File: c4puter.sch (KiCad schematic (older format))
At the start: 1 part, among them J7 19V 3A

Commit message: Uh, more misc work.
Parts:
- added C1: 1u, IPC7351-Nominal:CAPC2012X70, symbol C-0805
- added C2: 100n, IPC7351-Nominal:CAPC1005X55, symbol C-0402
- added Q1, Q2: AOD4189, smd-semi:TO-252, symbol AOD4189
- added R1: 100k, IPC7351-Nominal:RESC1608X50, symbol R-0603
- added R2: 330k, IPC7351-Nominal:RESC1608X50, symbol R-0603
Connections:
- net labels added: +12, 12VIN
- net labels removed: V+
- wire segments 22 -> 41
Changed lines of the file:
@@
 $Descr A4 11693 8268
 encoding utf-8
-Sheet 1 8
+Sheet 1 9
 Title ""
 Date ""
@@
 $EndComp
 Wire Wire Line
-	1200 800  1300 800
-$Comp
-L V+ #PWR2
-U 1 1 5765EDAE
-P 1300 800
-F 0 "#PWR2" H 1300 850 30  0001 C CNN
-F 1 "V+" V 1300 888 50  0000 L CNN
-F 2 "" H 1300 800 60  0000 C CNN
-F 3 "" H 1300 800 60  0000 C CNN
-	1    1300 800
-	0    1    1    0
-$EndComp
+	1200 800  1500 800
 $Comp
 L GND #PWR1
@@
 F1 "Power.sch" 60
 $EndSheet
+$Comp
+L AOD4189 Q2
+U 1 1 577BAA66
+P 2600 850
+F 0 "Q2" V 2864 850 50  0000 C CNN
+F 1 "AOD4189" V 2773 850 50  0000 C CNN
+F 2 "smd-semi:TO-252" H 2600 600 50  0001 C CNN
+F 3 "http://aosmd.com/res/data_sheets/AOD4189.pdf" H 2600 700 60  0001 C CNN
+F 4 "PMOS AOS AOD4189" H 2600 500 60  0001 C CNN "BOM"
+	1    2600 850
+	0    -1   -1   0
+$EndComp
+$Comp
+L AOD4189 Q1
+U 1 1 577BB49C
+P 1600 850
+F 0 "Q1" V 1864 850 50  0000 C CNN
+F 1 "AOD4189" V 1773 850 50  0000 C CNN
+F 2 "smd-semi:TO-252" H 1600 600 50  0001 C CNN
+F 3 "http://aosmd.com/res/data_sheets/AOD4189.pdf" H 1600 700 60  0001 C CNN
+F 4 "PMOS AOS AOD4189" H 1600 500 60  0001 C CNN "BOM"
+	1    1600 850
+	0    1    -1   0
+$EndComp
+Wire Wire Line
+	1700 800  1850 800
+Wire Wire Line
+	1850 800  2200 800
+Wire Wire Line
+	2200 800  2500 800
+Text GLabel 3100 800  2    50   Output ~ 0
++12
+Wire Wire Line
+	2700 800  2950 800
+Wire Wire Line
+	2950 800  3100 800
+Wire Wire Line
+	1650 900  1650 1100
+Wire Wire Line
+	1650 1100 1650 1200
+Wire Wire Line
+	1650 1100 1850 1100
+Wire Wire Line
+	1850 1100 2200 1100
+Wire Wire Line
+	2200 1100 2550 1100
+Wire Wire Line
+	2550 1100 2650 1100
+Wire Wire Line
+	2550 1100 2550 900
+$Comp
+L C-0805 C1
+U 1 1 577BC70C
+P 1850 950
+F 0 "C1" H 1963 996 50  0000 L CNN
+F 1 "1u" H 1963 905 50  0000 L CNN
+F 2 "IPC7351-Nominal:CAPC2012X70" H 1850 950 50  0001 C CNN
+F 3 "" H 1840 925 60  0000 C CNN
+F 4 "CAP MLCC 1u ≥X5R 16V 20% [0805]" H 2650 1500 60  0001 C CNN "BOM"
+	1    1850 950
+	1    0    0    -1
+$EndComp
+Wire Wire Line
+	1850 850  1850 800
+Connection ~ 1850 800
+Wire Wire Line
+	1850 1050 1850 1100
+Connection ~ 1850 1100
+$Comp
+L R-0603 R1
+U 1 1 577BD3FC
+P 1650 1300
+F 0 "R1" H 1713 1346 50  0000 L CNN
+F 1 "100k" H 1713 1255 50  0000 L CNN
+F 2 "IPC7351-Nominal:RESC1608X50" H 1650 1300 50  0001 C CNN
+F 3 "" H 1650 1350 60  0000 C CNN
+F 4 "RES SMD 100k 1% [0603]" H 2400 1850 60  0001 C CNN "BOM"
+	1    1650 1300
+	1    0    0    -1
+$EndComp
+Wire Wire Line
+	2200 800  2200 850
+Connection ~ 2200 800
+Wire Wire Line
+	2200 1050 2200 1100
+Connection ~ 2200 1100
+Connection ~ 1650 1100
+$Comp
+L R-0603 R2
+U 1 1 577BD8AB
+P 2200 950
+F 0 "R2" H 2263 996 50  0000 L CNN
+F 1 "330k" H 2263 905 50  0000 L CNN
+F 2 "IPC7351-Nominal:RESC1608X50" H 2200 950 50  0001 C CNN
+F 3 "" H 2200 1000 60  0000 C CNN
+F 4 "RES SMD 330k 1% [0603]" H 2950 1500 60  0001 C CNN "BOM"
+	1    2200 950
+	1    0    0    -1
+$EndComp
+$Comp
+L GND #PWR2
+U 1 1 577BDBFF
+P 1650 1450
+F 0 "#PWR2" H 1650 1450 30  0001 C CNN
+F 1 "GND" H 1650 1380 30  0001 C CNN
+F 2 "" H 1650 1450 60  0000 C CNN
+F 3 "" H 1650 1450 60  0000 C CNN
+	1    1650 1450
+	1    0    0    -1
+$EndComp
+Wire Wire Line
+	1650 1450 1650 1400
+$Comp
+L C-0402 C2
+U 1 1 577BE5F3
+P 2750 1100
+F 0 "C2" V 2908 1100 50  0000 C CNN
+F 1 "100n" V 2999 1100 50  0000 C CNN
+F 2 "IPC7351-Nominal:CAPC1005X55" H 2750 1100 50  0001 C CNN
+F 3 "" H 2740 1075 60  0000 C CNN
+F 4 "CAP MLCC 100n ≥X5R 25V 10% [0402]" H 3550 1650 60  0001 C CNN "BOM"
+	1    2750 1100
+	0    1    1    0
+$EndComp
+Connection ~ 2550 1100
+Wire Wire Line
+	2950 800  2950 1100
+Wire Wire Line
+	2950 1100 2850 1100
+Connection ~ 2950 800
+Text Label 1250 800  0    50   ~ 0
+12VIN
+$Sheet
+S 4300 4700 1300 900
+U 577C2AEA
+F0 "Blinkenlights" 50
+F1 "Blinkenlights.sch" 50
+$EndSheet
 $EndSCHEMATC

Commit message: MOAR WORK
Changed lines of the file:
@@
 $EndComp
 Wire Wire Line
-	1700 800  1850 800
-Wire Wire Line
-	1850 800  2200 800
-Wire Wire Line
-	2200 800  2500 800
+	1700 800  2500 800
 Text GLabel 3100 800  2    50   Output ~ 0
 +12
 Wire Wire Line
-	2700 800  2950 800
+	2700 800  3100 800
 Wire Wire Line
-	2950 800  3100 800
+	1650 900  1650 1200
 Wire Wire Line
-	1650 900  1650 1100
-Wire Wire Line
-	1650 1100 1650 1200
-Wire Wire Line
-	1650 1100 1850 1100
-Wire Wire Line
-	1850 1100 2200 1100
-Wire Wire Line
-	2200 1100 2550 1100
-Wire Wire Line
-	2550 1100 2650 1100
+	1650 1100 2650 1100
 Wire Wire Line
 	2550 1100 2550 900

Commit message: MOAR WORK, v2
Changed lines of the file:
@@
 F14 "CPUASTR" B R 6100 3600 50
 F15 "CPUDSTR" B R 6100 3700 50
+F16 "LIMBD[0..7]" B L 4700 3500 50
+F17 "LIMBA15" I L 4700 3600 50
+F18 "LIMBNCS" I L 4700 3700 50
+F19 "LIMBNRD" I L 4700 3900 50
+F20 "LIMBNWAIT" O L 4700 4000 50
+F21 "LIMBNWE" I L 4700 3800 50
 $EndSheet
 $Sheet
@@
 F0 "EC" 60
 F1 "EC.sch" 60
+F2 "D[0..7]" B R 3200 4800 50
+F3 "A15" O R 3200 4900 50
+F4 "NCS" O R 3200 5000 50
+F5 "NWE" O R 3200 5100 50
+F6 "NRD" O R 3200 5200 50
+F7 "NWAIT" O R 3200 5300 50
 $EndSheet
 $Comp
@@
 F1 "Blinkenlights.sch" 50
 $EndSheet
+Wire Bus Line
+	4700 3500 3400 3500
+Wire Bus Line
+	3400 3500 3400 4800
+Wire Bus Line
+	3400 4800 3200 4800
+Wire Wire Line
+	3200 4900 3500 4900
+Wire Wire Line
+	3500 4900 3500 3600
+Wire Wire Line
+	3500 3600 4700 3600
+Wire Wire Line
+	4700 3700 3600 3700
+Wire Wire Line
+	3600 3700 3600 5000
+Wire Wire Line
+	3600 5000 3200 5000
+Wire Wire Line
+	3200 5100 3700 5100
+Wire Wire Line
+	3700 5100 3700 3800
+Wire Wire Line
+	3700 3800 4700 3800
+Wire Wire Line
+	4700 3900 3800 3900
+Wire Wire Line
+	3800 3900 3800 5200
+Wire Wire Line
+	3800 5200 3200 5200
+Wire Wire Line
+	3200 5300 3900 5300
+Wire Wire Line
+	3900 5300 3900 4000
+Wire Wire Line
+	3900 4000 4700 4000
 $EndSCHEMATC

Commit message: workworkwork
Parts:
- added MP1, MP2, MP3, MP4: SCREW, mech:SCREW-4-SUPPORTED, symbol SCREW
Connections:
- net GND: now also MP1.1, MP2.1, MP3.1, MP4.1

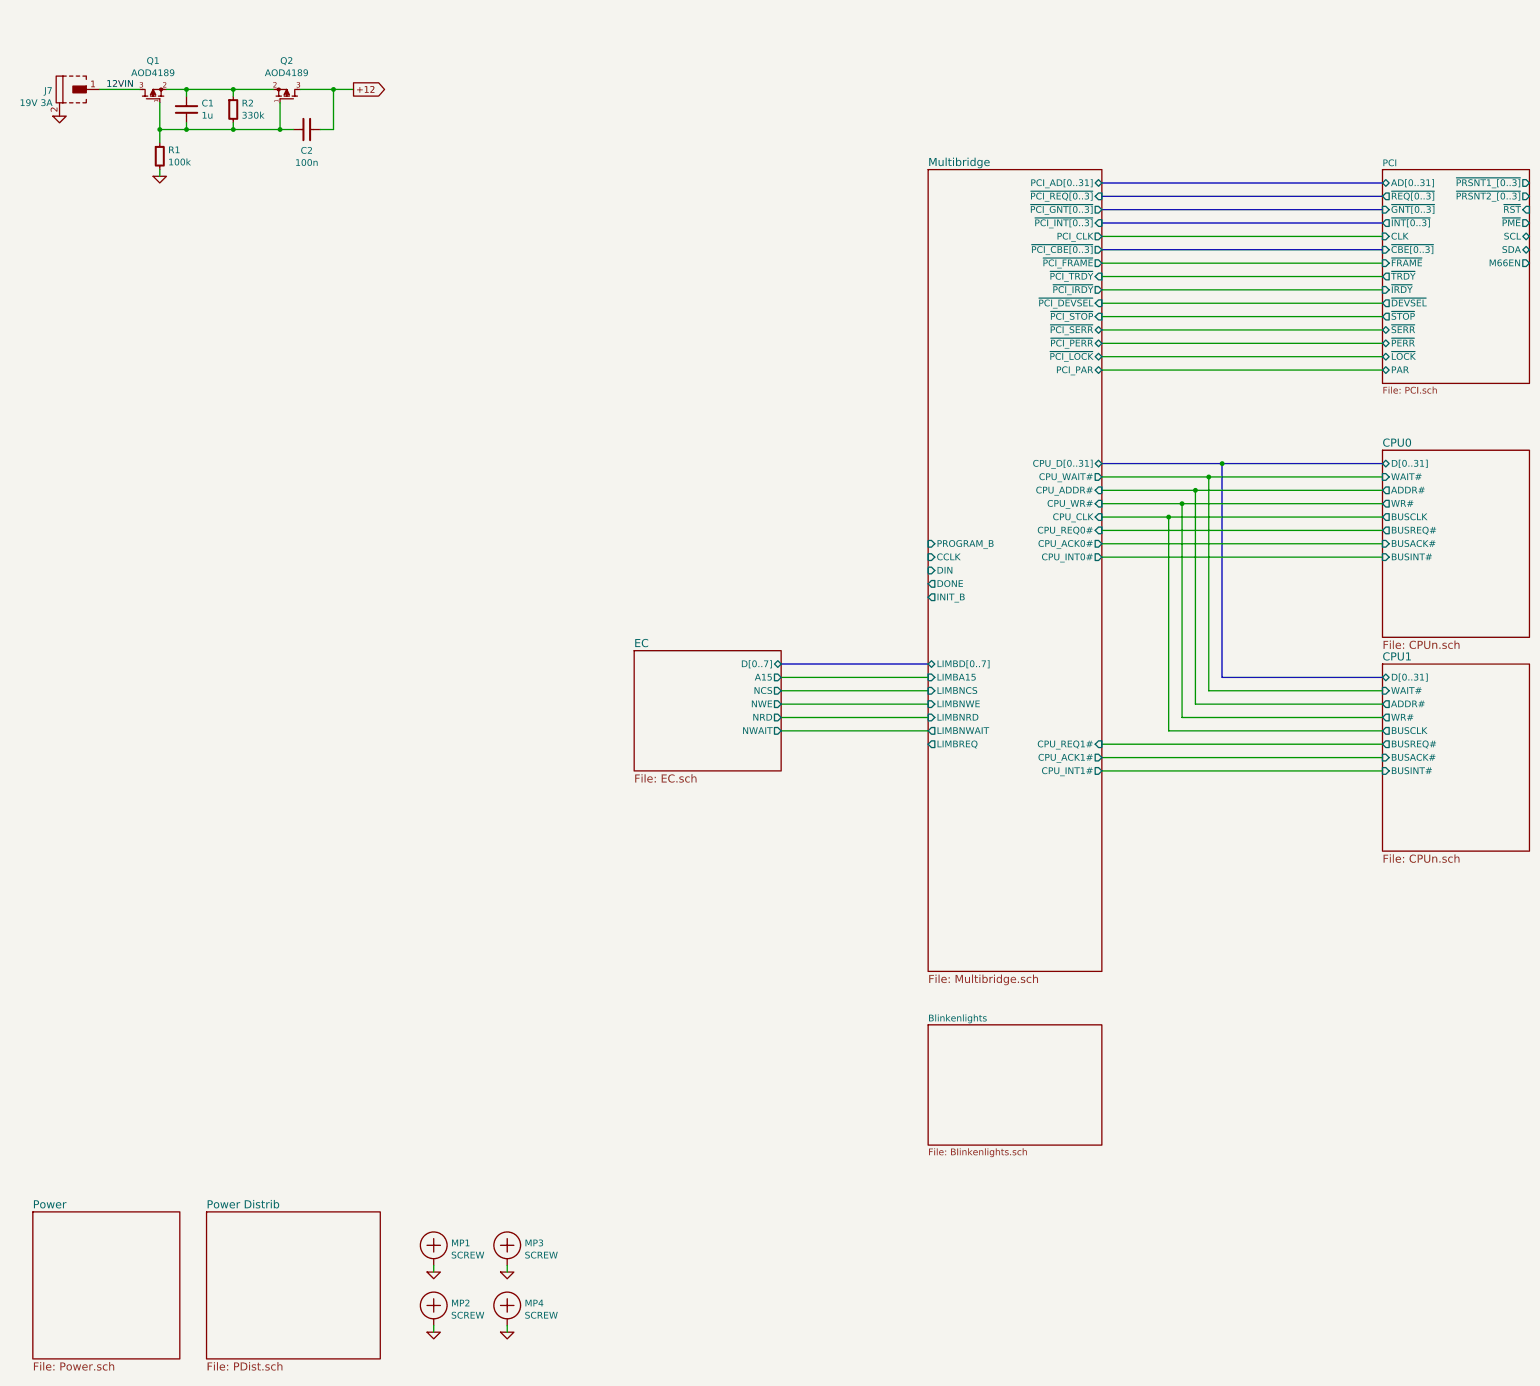
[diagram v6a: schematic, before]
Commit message: Route CPU bus and cache
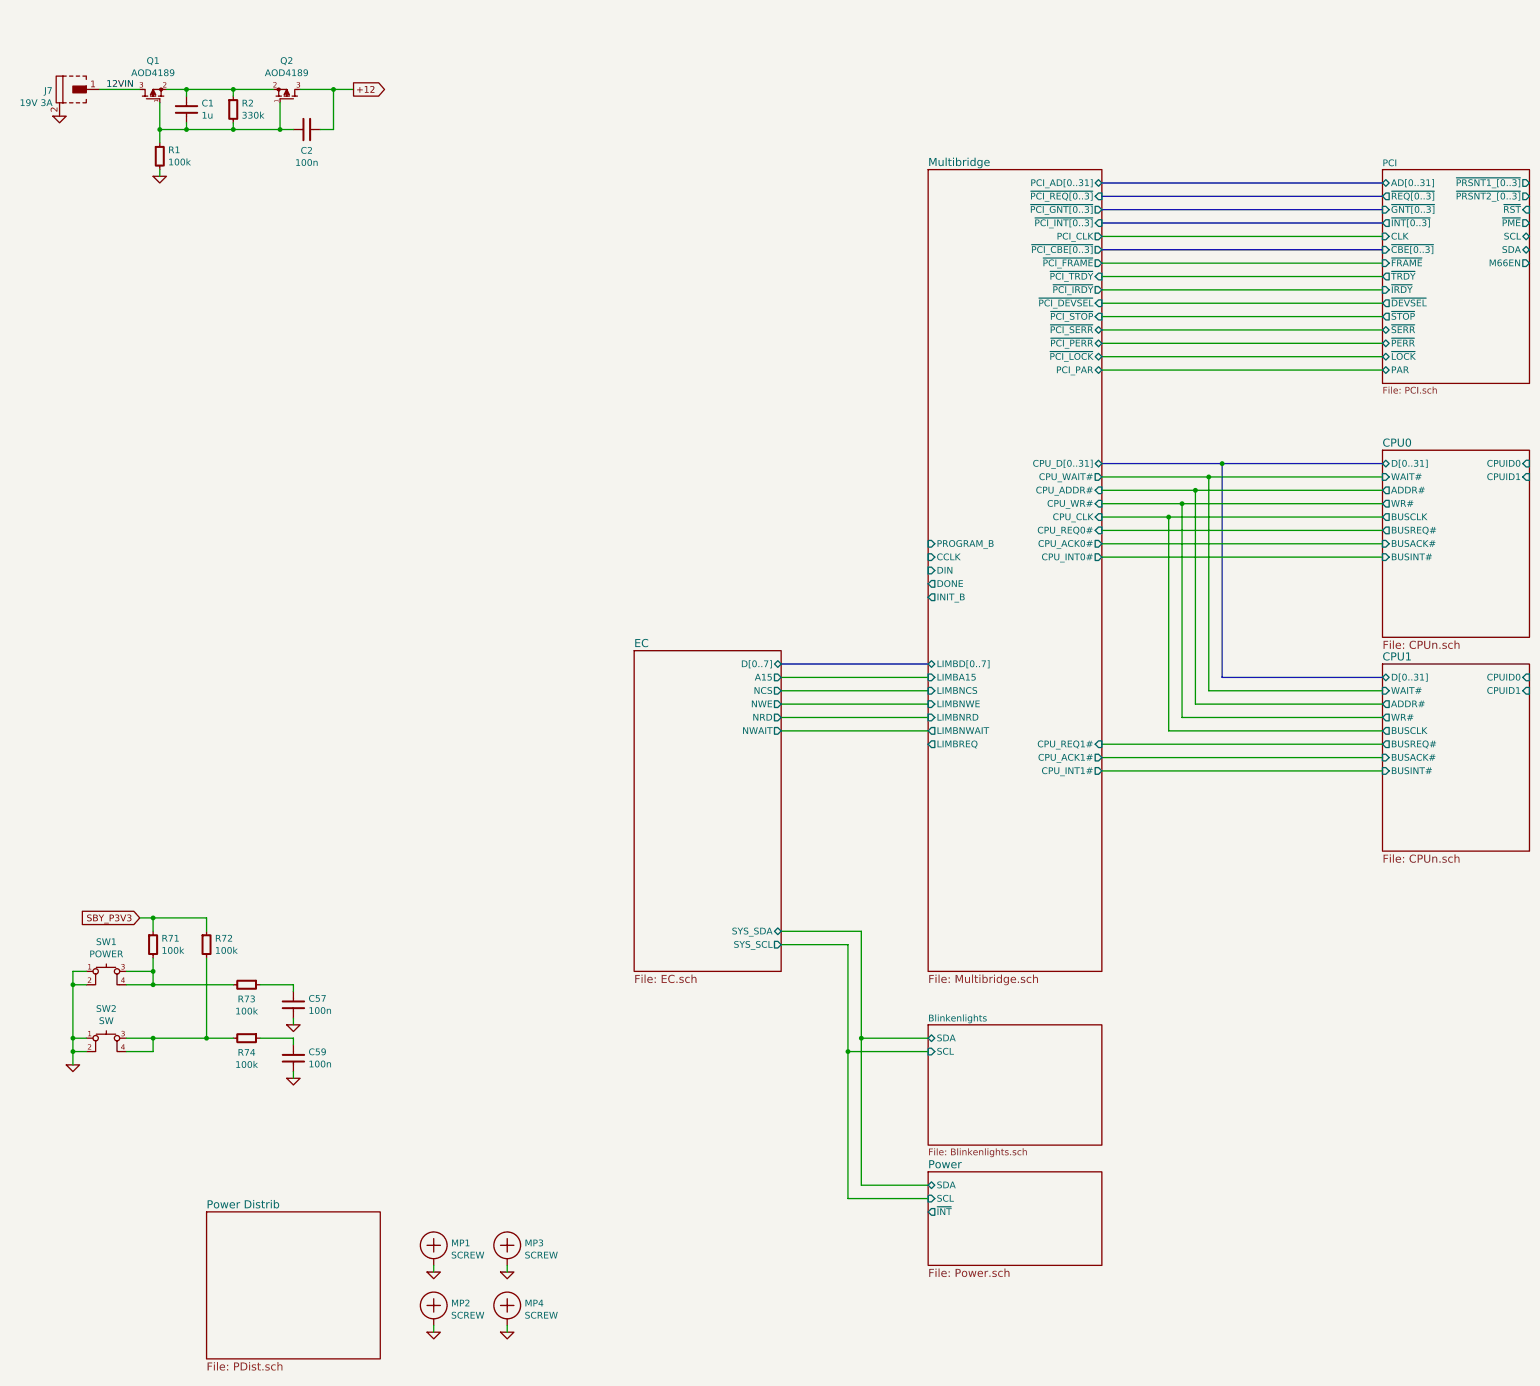
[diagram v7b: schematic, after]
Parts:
- added C57, C59: 100n, IPC7351-Nominal:CAPC1005X55, symbol C-0402
- added R71, R72, R73, R74: 100k, IPC7351-Nominal:RESC1608X50, symbol R-0603
- added SW1: POWER, manuf:CK-PTS645-SMD, symbol TACT-CK-PTS645-SMD
- added SW2: SW, manuf:CK-PTS645-SMD, symbol TACT-CK-PTS645-SMD
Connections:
- net GND: now also C57.2, C59.2, SW1.1, SW1.2, SW2.1, SW2.2
- new net: R71.2, R73.2, SW1.3, SW1.4
- new net: R72.2, R74.2, SW2.3, SW2.4
- new net: C57.1, R73.1
- new net: C59.1, R74.1
- new net SBY_P3V3: R71.1, R72.1

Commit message: workworkwork
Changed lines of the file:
@@
 $Descr B 17000 11000
 encoding utf-8
-Sheet 1 9
+Sheet 1 10
 Title ""
 Date ""
@@
 $EndDescr
 $Sheet
-S 2000 9200 1300 1100
+S 9100 9200 1300 1100
 U 5763AB3B
 F0 "Power Distrib" 60
@@
 $EndComp
 $Sheet
-S 7400 8900 1300 700
+S 7400 9600 1300 700
 U 5765C2BD
 F0 "Power" 60
 F1 "Power.sch" 60
-F2 "SCL" I L 7400 9100 50
-F3 "SDA" B L 7400 9000 50
-F4 "~INT" O L 7400 9200 50
+F2 "SCL" I L 7400 9800 50
+F3 "SDA" B L 7400 9700 50
+F4 "~INT" O L 7400 9900 50
 $EndSheet
 $Comp
@@
 12VIN
 $Sheet
-S 7400 7800 1300 900
+S 7400 8500 1300 900
 U 577C2AEA
 F0 "Blinkenlights" 50
 F1 "Blinkenlights.sch" 50
-F2 "SDA" B L 7400 7900 50
-F3 "SCL" I L 7400 8000 50
+F2 "SDA" B L 7400 8600 50
+F3 "SCL" I L 7400 8700 50
 $EndSheet
 $Sheet
@@
 	6300 7100 6900 7100
 Wire Wire Line
-	6900 7100 6900 9000
-Wire Wire Line
-	6900 7900 7400 7900
-Wire Wire Line
-	7400 8000 6800 8000
-Wire Wire Line
-	6800 7200 6800 9100
+	6900 7100 6900 9700
+Wire Wire Line
+	6900 8600 7400 8600
+Wire Wire Line
+	7400 8700 6800 8700
+Wire Wire Line
+	6800 7200 6800 9800
 Wire Wire Line
 	6800 7200 6300 7200
 Wire Wire Line
-	6900 9000 7400 9000
-Connection ~ 6900 7900
-Wire Wire Line
-	6800 9100 7400 9100
-Connection ~ 6800 8000
+	6900 9700 7400 9700
+Connection ~ 6900 8600
+Wire Wire Line
+	6800 9800 7400 9800
+Connection ~ 6800 8700
+$Sheet
+S 7400 7600 1300 700
+U 57981212
+F0 "Misc" 50
+F1 "Misc.sch" 50
+F2 "SDA" B L 7400 7700 50
+F3 "SCL" I L 7400 7800 50
+$EndSheet
+Wire Wire Line
+	7400 7700 6900 7700
+Connection ~ 6900 7700
+Wire Wire Line
+	7400 7800 6800 7800
+Connection ~ 6800 7800
 $EndSCHEMATC
